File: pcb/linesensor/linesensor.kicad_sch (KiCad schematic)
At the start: 3 parts, among them J1 Conn_01x03_Socket

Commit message: linesensor new
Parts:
- added U1: TRCT5000, Library:CRT5000, symbol 4xxx_IEEE:4049
- R1: value 220 -> R; footprint Resistor_THT:R_Axial_DIN0207_L6.3mm_D2.5mm_P7.62mm_Horizontal -> Resistor_THT:R_Axial_DIN0309_L9.0mm_D3.2mm_P12.70mm_Horizontal
- R2: value 4,7 -> R; footprint Resistor_THT:R_Axial_DIN0207_L6.3mm_D2.5mm_P7.62mm_Horizontal -> Resistor_THT:R_Axial_DIN0309_L9.0mm_D3.2mm_P12.70mm_Horizontal
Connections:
- net GND: now also J1.2 (Pin_2), U1.4 (Vss); no longer J1.3 (Pin_3), R2.1
- net at J1.1 (Pin_1): now also R1.2, U1.2; no longer R1.1
- net at R2.2: now also J1.3 (Pin_3); no longer R1.2
- new net: R2.1, U1.3
- new net: R1.1, U1.1 (Vdd)

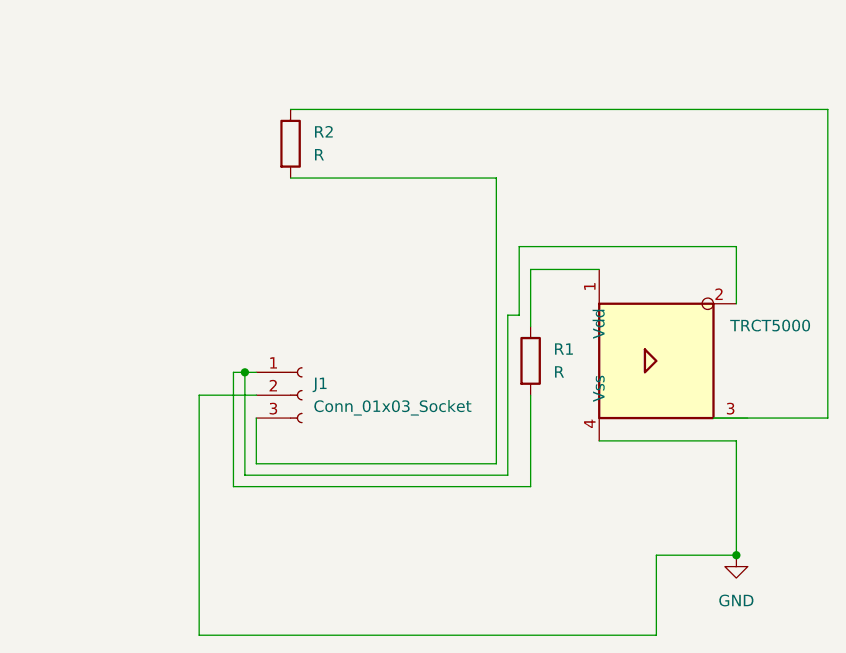
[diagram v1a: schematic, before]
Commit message: fixed line sensor PCB
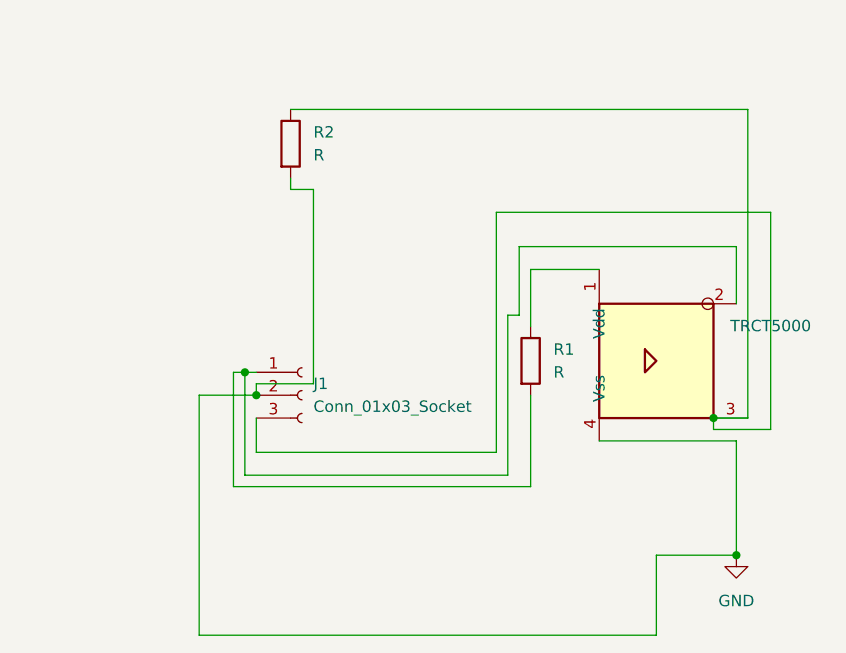
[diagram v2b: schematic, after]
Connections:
- net GND: now also R2.2
- net at R2.1, U1.3: now also J1.3 (Pin_3)
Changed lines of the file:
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@@
 	(paper "A4")
 	(junction
+		(at 96.52 66.04)
+		(diameter 0)
+		(color 0 0 0 0)
+	)
+	(junction
+		(at 45.72 63.5)
+		(diameter 0)
+		(color 0 0 0 0)
+	)
+	(junction
 		(at 44.45 60.96)
 		(diameter 0)
@@
 	(wire
 		(pts
-			(xy 72.39 39.37) (xy 72.39 71.12)
+			(xy 72.39 43.18) (xy 102.87 43.18)
+		)
+		(stroke
+			(width 0)
+			(type default)
+		)
+	)
+	(wire
+		(pts
+			(xy 45.72 66.04) (xy 45.72 69.85)
+		)
+		(stroke
+			(width 0)
+			(type default)
+		)
+	)
+	(wire
+		(pts
+			(xy 102.87 67.31) (xy 96.52 67.31)
 		)
 		(stroke
@@
 	(wire
 		(pts
-			(xy 72.39 39.37) (xy 49.53 39.37)
-		)
-		(stroke
-			(width 0)
-			(type default)
-		)
-	)
-	(wire
-		(pts
 			(xy 44.45 60.96) (xy 44.45 72.39)
 		)
@@
 	(wire
 		(pts
-			(xy 45.72 71.12) (xy 72.39 71.12)
-		)
-		(stroke
-			(width 0)
-			(type default)
-		)
-	)
-	(wire
-		(pts
 			(xy 76.2 55.88) (xy 76.2 49.53)
 		)
@@
 	(wire
 		(pts
+			(xy 45.72 62.23) (xy 52.07 62.23)
+		)
+		(stroke
+			(width 0)
+			(type default)
+		)
+	)
+	(wire
+		(pts
+			(xy 96.52 67.31) (xy 96.52 66.04)
+		)
+		(stroke
+			(width 0)
+			(type default)
+		)
+	)
+	(wire
+		(pts
+			(xy 100.33 31.75) (xy 100.33 66.04)
+		)
+		(stroke
+			(width 0)
+			(type default)
+		)
+	)
+	(wire
+		(pts
 			(xy 74.93 46.99) (xy 74.93 54.61)
 		)
@@
 	(wire
 		(pts
+			(xy 49.53 40.64) (xy 49.53 39.37)
+		)
+		(stroke
+			(width 0)
+			(type default)
+		)
+	)
+	(wire
+		(pts
+			(xy 100.33 66.04) (xy 96.52 66.04)
+		)
+		(stroke
+			(width 0)
+			(type default)
+		)
+	)
+	(wire
+		(pts
+			(xy 45.72 63.5) (xy 45.72 62.23)
+		)
+		(stroke
+			(width 0)
+			(type default)
+		)
+	)
+	(wire
+		(pts
 			(xy 39.37 63.5) (xy 39.37 90.17)
 		)
@@
 	(wire
 		(pts
-			(xy 49.53 31.75) (xy 109.22 31.75)
+			(xy 52.07 62.23) (xy 52.07 40.64)
+		)
+		(stroke
+			(width 0)
+			(type default)
+		)
+	)
+	(wire
+		(pts
+			(xy 72.39 69.85) (xy 72.39 43.18)
 		)
 		(stroke
@@
 	(wire
 		(pts
-			(xy 109.22 31.75) (xy 109.22 66.04)
-		)
-		(stroke
-			(width 0)
-			(type default)
-		)
-	)
-	(wire
-		(pts
-			(xy 109.22 66.04) (xy 96.52 66.04)
-		)
-		(stroke
-			(width 0)
-			(type default)
-		)
-	)
-	(wire
-		(pts
 			(xy 43.18 60.96) (xy 44.45 60.96)
 		)
@@
 	(wire
 		(pts
+			(xy 52.07 40.64) (xy 49.53 40.64)
+		)
+		(stroke
+			(width 0)
+			(type default)
+		)
+	)
+	(wire
+		(pts
 			(xy 99.06 53.34) (xy 99.06 46.99)
 		)
@@
 	(wire
 		(pts
+			(xy 102.87 43.18) (xy 102.87 67.31)
+		)
+		(stroke
+			(width 0)
+			(type default)
+		)
+	)
+	(wire
+		(pts
 			(xy 74.93 54.61) (xy 73.66 54.61)
 		)
@@
 	(wire
 		(pts
-			(xy 45.72 66.04) (xy 45.72 71.12)
-		)
-		(stroke
-			(width 0)
-			(type default)
-		)
-	)
-	(wire
-		(pts
 			(xy 76.2 73.66) (xy 76.2 63.5)
 		)
@@
 	(wire
 		(pts
+			(xy 49.53 31.75) (xy 100.33 31.75)
+		)
+		(stroke
+			(width 0)
+			(type default)
+		)
+	)
+	(wire
+		(pts
 			(xy 43.18 60.96) (xy 43.18 73.66)
 		)
@@
 		)
 		(stroke
+			(width 0)
+			(type default)
+		)
+	)
+	(wire
+		(pts
+			(xy 45.72 69.85) (xy 72.39 69.85)
+		)
+		(stroke
